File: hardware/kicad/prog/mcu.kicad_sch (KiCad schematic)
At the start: 23 parts, among them J4 microSD, J5 Câble PROG-CHA, SW1 Retour menu

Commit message: Pico 2, microSD et bouton sur la carte PROG ; pistes d'alimentation larges
- La carte PROG est côté avant de la cartouche, composants vers l'avant :
  lecteur microSD et bouton accessibles. Le câble PROG-CHA porte
  désormais le bus de liaison C/SM ; connecteur au même endroit sur les
  deux cartes (x = 172 mm), prêt pour un connecteur carte à carte.
- Sous le Pico : ni piste ni via sur la face composants (pastilles de
  test nues sous le module).
- Classes de réseaux écrites dans le .kicad_pro : +5V et VSYS en 0,5 mm,
  +1V2 en 0,3 mm.
- Broches des FPGA réoptimisées ; contrôle Freerouting sans violation ;
  routage des deux cartes et vérification de timing en cours.

Co-Authored-By: Claude Opus 5.5 <noreply@anthropic.com>
Claude-Session: https://claude.ai/code/session_01WKfXP1YJ8otGxZ5dsY6Agh
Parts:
- removed C73: 10u, Capacitor_SMD:C_0805_2012Metric, symbol Device:C
- removed C74: 100n, Capacitor_SMD:C_0603_1608Metric, symbol Device:C
- removed D2: SS14 / BAT60A, Diode_SMD:D_SOD-123, symbol Device:D_Schottky
- removed J4: microSD, Connector_Card:microSD_HC_Wuerth_693072010801, symbol Connector:Micro_SD_Card
- removed J5: Câble PROG-CHA, Connector_PinHeader_2.54mm:PinHeader_2x07_P2.54mm_Vertical, symbol Connector_Generic:Conn_02x07_Odd_Even
- removed R13, R14, R15, R16, R17, R18, R19: 33, Resistor_SMD:R_0603_1608Metric, symbol Device:R
- added C75: 10u, Capacitor_SMD:C_0805_2012Metric, symbol Device:C
- added C76: 100n, Capacitor_SMD:C_0603_1608Metric, symbol Device:C
- added D3: SS14 / BAT60A, Diode_SMD:D_SOD-123, symbol Device:D_Schottky
- added J5: microSD, Connector_Card:microSD_HC_Wuerth_693072010801, symbol Connector:Micro_SD_Card
- added R29: 33, Resistor_SMD:R_0603_1608Metric, symbol Device:R
- added R30, R31, R32, R33, R34: 10k, Resistor_SMD:R_0603_1608Metric, symbol Device:R
- R23, R24, R25, R26, R27, R28: value 10k -> 33
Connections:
- net +3V3: now also C75.1, C76.1, J5.4 (VDD), R30.1, R31.1, R32.1, R33.1, R34.1; no longer R23.1, R24.1, R25.1, R26.1, R27.1, R28.1
- net +5V: now also D3.2 (A)
- net CDONE: no longer R23.2
- net CHA_IO0: now also R26.2
- net CHA_IO0_MCU: now also R26.1
- net CHA_IO1: now also R27.2; no longer R20.2
- net CHA_IO1_MCU: now also R27.1; no longer R20.1
- net CHA_IO2: now also R28.2; no longer R21.2
- net CHA_IO2_MCU: now also R28.1; no longer R21.1
- net CHA_IO3: now also R29.2; no longer R22.2
- net CHA_IO3_MCU: now also R29.1; no longer R22.1
- net CHA_SCK: now also R25.2
- net CHA_SCK_MCU: now also R25.1
- net GND: now also C75.2, C76.2, J5.6 (VSS), J5.9 (SHIELD)
- net PICO_VSYS: now also D3.1 (K)
- net PROG_IO0: now also R21.2
- net PROG_IO0_MCU: now also R21.1
- net PROG_IO1: now also R22.2
- net PROG_IO1_MCU: now also R22.1
- net PROG_IO2: now also R23.2
- net PROG_IO2_MCU: now also R23.1
- net PROG_IO3: now also R24.2
- net PROG_IO3_MCU: now also R24.1
- net PROG_SCK: now also R20.2
- net PROG_SCK_MCU: now also R20.1
- net SD_CLK: now also J5.5 (CLK)
- net SD_CMD: now also J5.3 (CMD), R30.2; no longer R24.2
- net SD_D0: now also J5.7 (DAT0), R31.2; no longer R25.2
- net SD_D1: now also J5.8 (DAT1), R32.2; no longer R26.2
- net SD_D2: now also J5.1 (DAT2), R33.2; no longer R27.2
- net SD_D3: now also J5.2 (DAT3/CD), R34.2; no longer R28.2
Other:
- title: SDAES - carte CHA (sprites, couche fixe, Z80, RP2350) - RP2350, carte SD, câble -> SDAES - carte PROG (programme 68000 + son ADPCM) - RP2350, carte SD, bouton

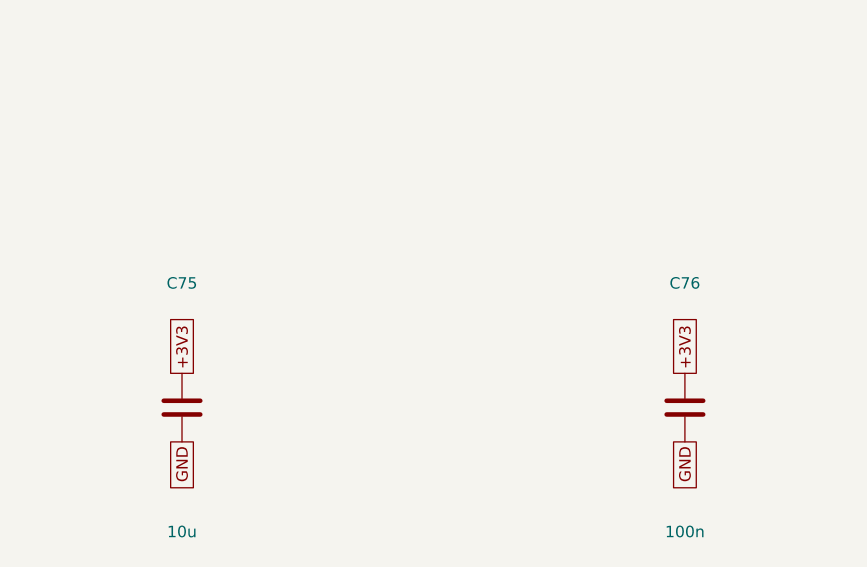
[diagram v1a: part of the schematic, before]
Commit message: Régulateur 3,3 V à découpage, horloge SDRAM adaptée côté FPGA, U8 en 74AHCT125
- AP63203 (TSOT-23-6, sortie fixe 3,3 V, ~90 %) à la place de
  l'AMS1117 : ~0,15 W de pertes au lieu de ~0,75 W et moins de courant
  tiré sur le 5 V de la console ; L 4,7 µH, Cin 10 µF, Cout 2 x 22 µF.
- Résistance série de 33 ohms de l'horloge SDRAM déclarée avec le FPGA :
  placée à 2,7 mm de sa broche (au lieu de ~30 mm, côté SDRAM).
- CHA : U8 (16244 pour 2 canaux) remplacé par un 74AHCT125.
Cartes replacées, contrôle Freerouting sans violation ; routage des
deux cartes et vérification de timing en cours.

Co-Authored-By: Claude Opus 5.5 <noreply@anthropic.com>
Claude-Session: https://claude.ai/code/session_01WKfXP1YJ8otGxZ5dsY6Agh
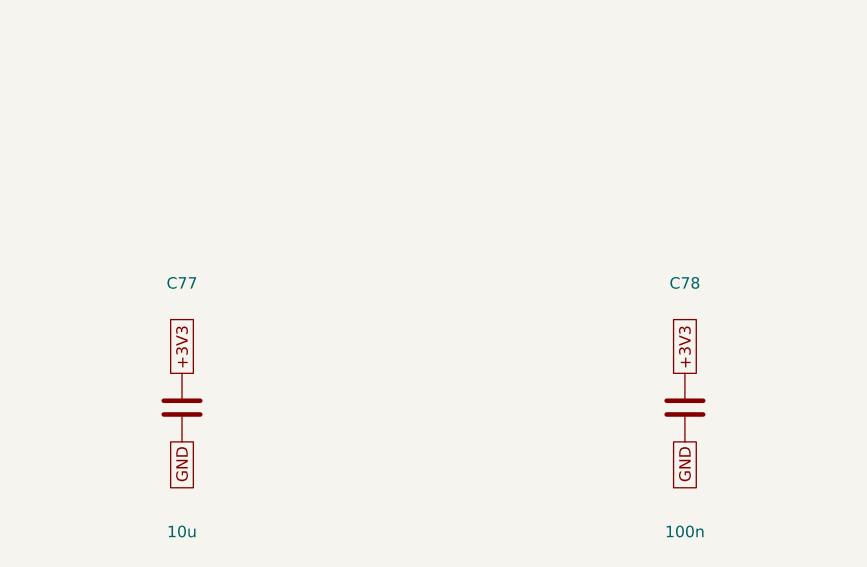
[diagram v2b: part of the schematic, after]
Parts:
- removed C75: 10u, Capacitor_SMD:C_0805_2012Metric, symbol Device:C
- removed C76: 100n, Capacitor_SMD:C_0603_1608Metric, symbol Device:C
- added C77: 10u, Capacitor_SMD:C_0805_2012Metric, symbol Device:C
- added C78: 100n, Capacitor_SMD:C_0603_1608Metric, symbol Device:C
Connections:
- net +3V3: now also C77.1, C78.1
- net GND: now also C77.2, C78.2
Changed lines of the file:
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@@
     (instances
       (project "prog"
-        (path "/730f52e2-cd0f-4a48-866b-cc2c9ca510b4/304ee4f0-0a6a-4b03-9db8-8e738f6a2d8a"
+        (path "/3a034faf-f518-4ff2-b4c3-d71a1132e6ac/1c05fe67-ad73-4d5e-9ba2-5b8f778208d5"
           (reference "A1")
           (unit 1)))))
@@
     (instances
       (project "prog"
-        (path "/730f52e2-cd0f-4a48-866b-cc2c9ca510b4/304ee4f0-0a6a-4b03-9db8-8e738f6a2d8a"
+        (path "/3a034faf-f518-4ff2-b4c3-d71a1132e6ac/1c05fe67-ad73-4d5e-9ba2-5b8f778208d5"
           (reference "D3")
           (unit 1)))))
@@
     (instances
       (project "prog"
-        (path "/730f52e2-cd0f-4a48-866b-cc2c9ca510b4/304ee4f0-0a6a-4b03-9db8-8e738f6a2d8a"
+        (path "/3a034faf-f518-4ff2-b4c3-d71a1132e6ac/1c05fe67-ad73-4d5e-9ba2-5b8f778208d5"
           (reference "R20")
           (unit 1)))))
@@
     (instances
       (project "prog"
-        (path "/730f52e2-cd0f-4a48-866b-cc2c9ca510b4/304ee4f0-0a6a-4b03-9db8-8e738f6a2d8a"
+        (path "/3a034faf-f518-4ff2-b4c3-d71a1132e6ac/1c05fe67-ad73-4d5e-9ba2-5b8f778208d5"
           (reference "R21")
           (unit 1)))))
@@
     (instances
       (project "prog"
-        (path "/730f52e2-cd0f-4a48-866b-cc2c9ca510b4/304ee4f0-0a6a-4b03-9db8-8e738f6a2d8a"
+        (path "/3a034faf-f518-4ff2-b4c3-d71a1132e6ac/1c05fe67-ad73-4d5e-9ba2-5b8f778208d5"
           (reference "R22")
           (unit 1)))))
@@
     (instances
       (project "prog"
-        (path "/730f52e2-cd0f-4a48-866b-cc2c9ca510b4/304ee4f0-0a6a-4b03-9db8-8e738f6a2d8a"
+        (path "/3a034faf-f518-4ff2-b4c3-d71a1132e6ac/1c05fe67-ad73-4d5e-9ba2-5b8f778208d5"
           (reference "R23")
           (unit 1)))))
@@
     (instances
       (project "prog"
-        (path "/730f52e2-cd0f-4a48-866b-cc2c9ca510b4/304ee4f0-0a6a-4b03-9db8-8e738f6a2d8a"
+        (path "/3a034faf-f518-4ff2-b4c3-d71a1132e6ac/1c05fe67-ad73-4d5e-9ba2-5b8f778208d5"
           (reference "R24")
           (unit 1)))))
@@
     (instances
       (project "prog"
-        (path "/730f52e2-cd0f-4a48-866b-cc2c9ca510b4/304ee4f0-0a6a-4b03-9db8-8e738f6a2d8a"
+        (path "/3a034faf-f518-4ff2-b4c3-d71a1132e6ac/1c05fe67-ad73-4d5e-9ba2-5b8f778208d5"
           (reference "R25")
           (unit 1)))))
@@
     (instances
       (project "prog"
-        (path "/730f52e2-cd0f-4a48-866b-cc2c9ca510b4/304ee4f0-0a6a-4b03-9db8-8e738f6a2d8a"
+        (path "/3a034faf-f518-4ff2-b4c3-d71a1132e6ac/1c05fe67-ad73-4d5e-9ba2-5b8f778208d5"
           (reference "R26")
           (unit 1)))))
@@
     (instances
       (project "prog"
-        (path "/730f52e2-cd0f-4a48-866b-cc2c9ca510b4/304ee4f0-0a6a-4b03-9db8-8e738f6a2d8a"
+        (path "/3a034faf-f518-4ff2-b4c3-d71a1132e6ac/1c05fe67-ad73-4d5e-9ba2-5b8f778208d5"
           (reference "R27")
           (unit 1)))))
@@
     (instances
       (project "prog"
-        (path "/730f52e2-cd0f-4a48-866b-cc2c9ca510b4/304ee4f0-0a6a-4b03-9db8-8e738f6a2d8a"
+        (path "/3a034faf-f518-4ff2-b4c3-d71a1132e6ac/1c05fe67-ad73-4d5e-9ba2-5b8f778208d5"
           (reference "R28")
           (unit 1)))))
@@
     (instances
       (project "prog"
-        (path "/730f52e2-cd0f-4a48-866b-cc2c9ca510b4/304ee4f0-0a6a-4b03-9db8-8e738f6a2d8a"
+        (path "/3a034faf-f518-4ff2-b4c3-d71a1132e6ac/1c05fe67-ad73-4d5e-9ba2-5b8f778208d5"
           (reference "R29")
           (unit 1)))))
@@
     (instances
       (project "prog"
-        (path "/730f52e2-cd0f-4a48-866b-cc2c9ca510b4/304ee4f0-0a6a-4b03-9db8-8e738f6a2d8a"
+        (path "/3a034faf-f518-4ff2-b4c3-d71a1132e6ac/1c05fe67-ad73-4d5e-9ba2-5b8f778208d5"
           (reference "SW1")
           (unit 1)))))
@@
     (instances
       (project "prog"
-        (path "/730f52e2-cd0f-4a48-866b-cc2c9ca510b4/304ee4f0-0a6a-4b03-9db8-8e738f6a2d8a"
+        (path "/3a034faf-f518-4ff2-b4c3-d71a1132e6ac/1c05fe67-ad73-4d5e-9ba2-5b8f778208d5"
           (reference "J5")
           (unit 1)))))
@@
     (instances
       (project "prog"
-        (path "/730f52e2-cd0f-4a48-866b-cc2c9ca510b4/304ee4f0-0a6a-4b03-9db8-8e738f6a2d8a"
+        (path "/3a034faf-f518-4ff2-b4c3-d71a1132e6ac/1c05fe67-ad73-4d5e-9ba2-5b8f778208d5"
           (reference "R30")
           (unit 1)))))
@@
     (instances
       (project "prog"
-        (path "/730f52e2-cd0f-4a48-866b-cc2c9ca510b4/304ee4f0-0a6a-4b03-9db8-8e738f6a2d8a"
+        (path "/3a034faf-f518-4ff2-b4c3-d71a1132e6ac/1c05fe67-ad73-4d5e-9ba2-5b8f778208d5"
           (reference "R31")
           (unit 1)))))
@@
     (instances
       (project "prog"
-        (path "/730f52e2-cd0f-4a48-866b-cc2c9ca510b4/304ee4f0-0a6a-4b03-9db8-8e738f6a2d8a"
+        (path "/3a034faf-f518-4ff2-b4c3-d71a1132e6ac/1c05fe67-ad73-4d5e-9ba2-5b8f778208d5"
           (reference "R32")
           (unit 1)))))
@@
     (instances
       (project "prog"
-        (path "/730f52e2-cd0f-4a48-866b-cc2c9ca510b4/304ee4f0-0a6a-4b03-9db8-8e738f6a2d8a"
+        (path "/3a034faf-f518-4ff2-b4c3-d71a1132e6ac/1c05fe67-ad73-4d5e-9ba2-5b8f778208d5"
           (reference "R33")
           (unit 1)))))
@@
     (instances
       (project "prog"
-        (path "/730f52e2-cd0f-4a48-866b-cc2c9ca510b4/304ee4f0-0a6a-4b03-9db8-8e738f6a2d8a"
+        (path "/3a034faf-f518-4ff2-b4c3-d71a1132e6ac/1c05fe67-ad73-4d5e-9ba2-5b8f778208d5"
           (reference "R34")
           (unit 1)))))
@@
     (on_board yes)
     (dnp no)
-    (property "Reference" "C75"
+    (property "Reference" "C77"
       (at 492.76 103.03 0)
       (effects
@@
     (instances
       (project "prog"
-        (path "/730f52e2-cd0f-4a48-866b-cc2c9ca510b4/304ee4f0-0a6a-4b03-9db8-8e738f6a2d8a"
-          (reference "C75")
+        (path "/3a034faf-f518-4ff2-b4c3-d71a1132e6ac/1c05fe67-ad73-4d5e-9ba2-5b8f778208d5"
+          (reference "C77")
           (unit 1)))))
   (global_label "+3V3"
@@
     (on_board yes)
     (dnp no)
-    (property "Reference" "C76"
+    (property "Reference" "C78"
       (at 548.64 103.03 0)
       (effects
@@
     (instances
       (project "prog"
-        (path "/730f52e2-cd0f-4a48-866b-cc2c9ca510b4/304ee4f0-0a6a-4b03-9db8-8e738f6a2d8a"
-          (reference "C76")
+        (path "/3a034faf-f518-4ff2-b4c3-d71a1132e6ac/1c05fe67-ad73-4d5e-9ba2-5b8f778208d5"
+          (reference "C78")
           (unit 1)))))
   (global_label "+3V3"
